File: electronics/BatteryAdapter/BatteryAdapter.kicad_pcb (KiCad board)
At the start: 2 copper layers, 38 x 38 mm, 8 parts, among them J1 Conn_01x06_MountingPin, J2 Conn_01x02

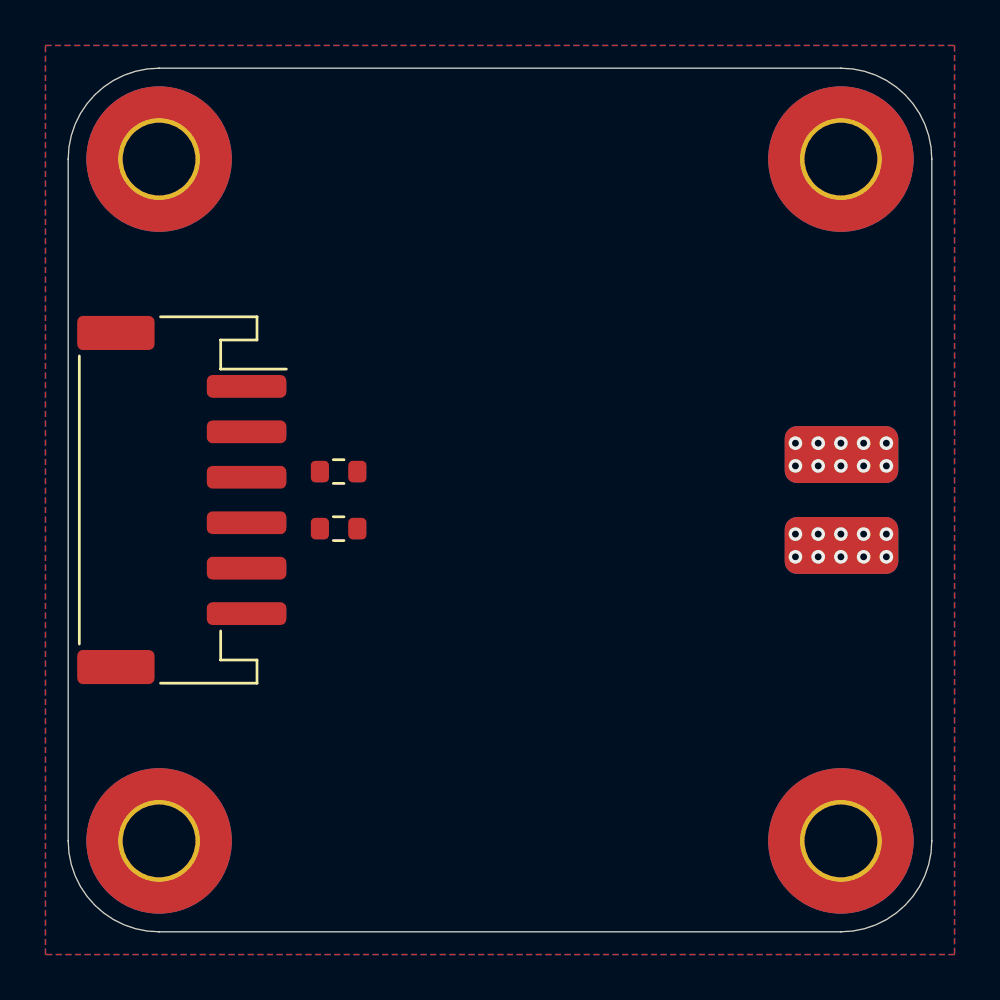
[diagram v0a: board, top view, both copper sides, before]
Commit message: electronics: fix battery adapter pins
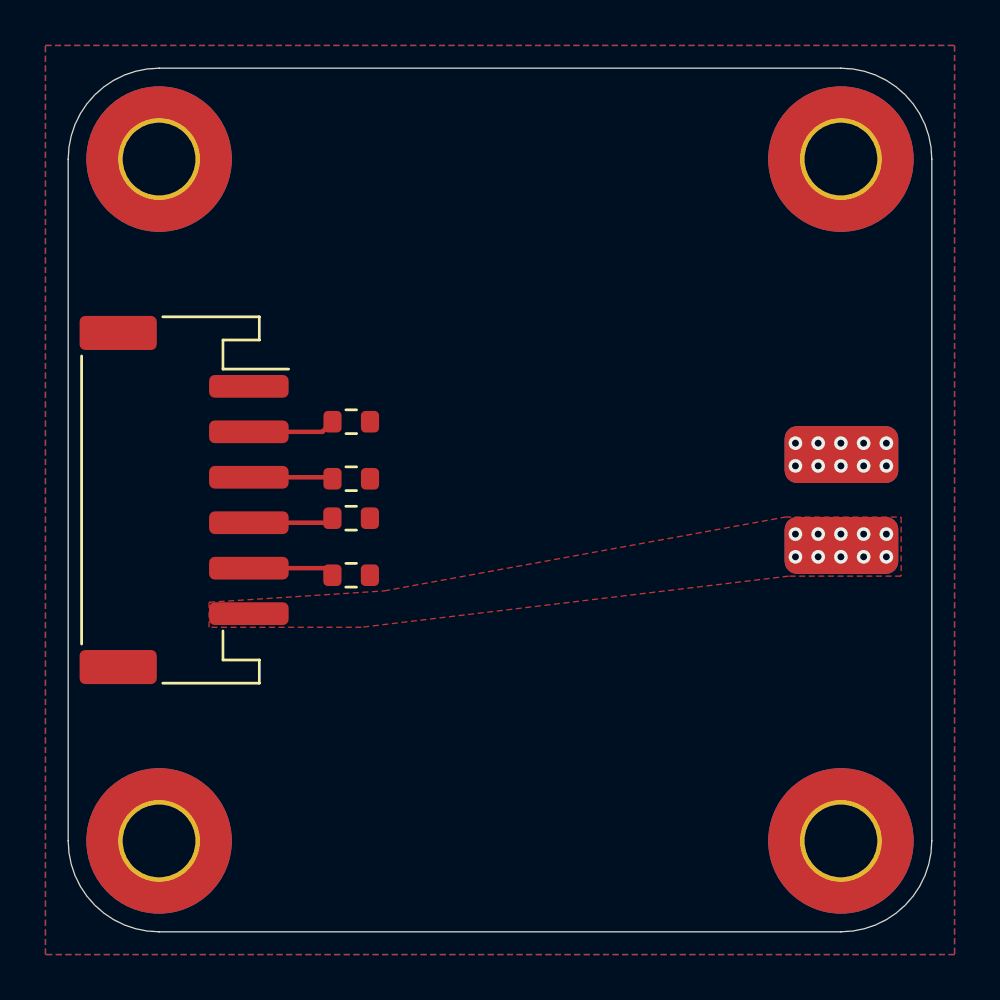
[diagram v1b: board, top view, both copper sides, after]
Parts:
- added R3: 5.1k, Resistor_SMD:R_0603_1608Metric, F.Cu at (108.5, 111.6)
- added R4: 5.1k, Resistor_SMD:R_0603_1608Metric, F.Cu at (108.5, 114.1)
- moved R1 2.12 mm to (108.5, 115.8)
- moved R2 2.12 mm to (108.5, 118.3)
- moved J1 0.10 mm to (101.1, 115.0)
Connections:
- J1 pad 2: unconnected-(J1-Pin_2-Pad2) -> /D+
- J1 pad 3: /CC2 -> /D-
- J1 pad 4: /CC1 -> /CC2
- J1 pad 5: unconnected-(J1-Pin_5-Pad5) -> /CC1
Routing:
- net /D+: track 0.00 -> 3.86 mm
- net /CC1: track 0.00 -> 3.80 mm
- net /CC2: track 0.00 -> 3.76 mm
- net /D-: track 0.00 -> 3.71 mm
- added copper zone on F.Cu, net VBUS
